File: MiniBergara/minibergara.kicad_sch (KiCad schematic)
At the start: 12 parts, among them SW1 SW_Nidec_CAS-120A1, U1 TB6612_BREAKOUT, U3 AMS1117-1.5

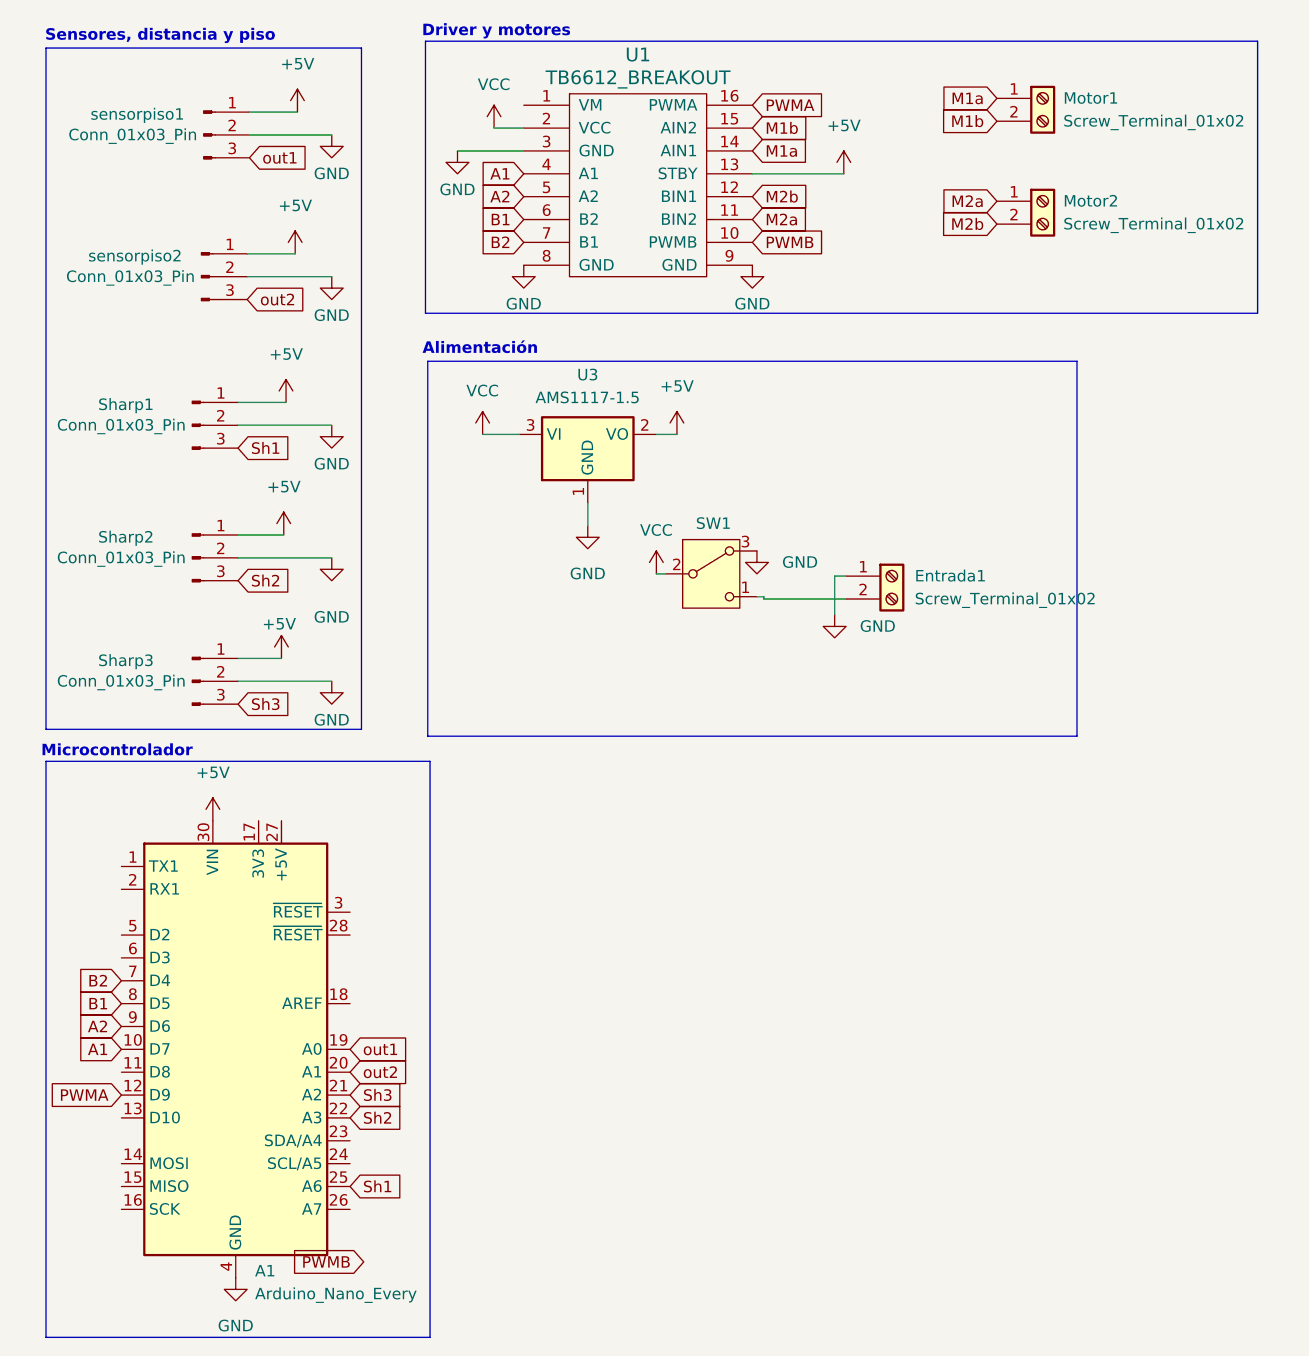
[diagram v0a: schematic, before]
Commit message: falta mover nano
move el nano abajo con las pistas
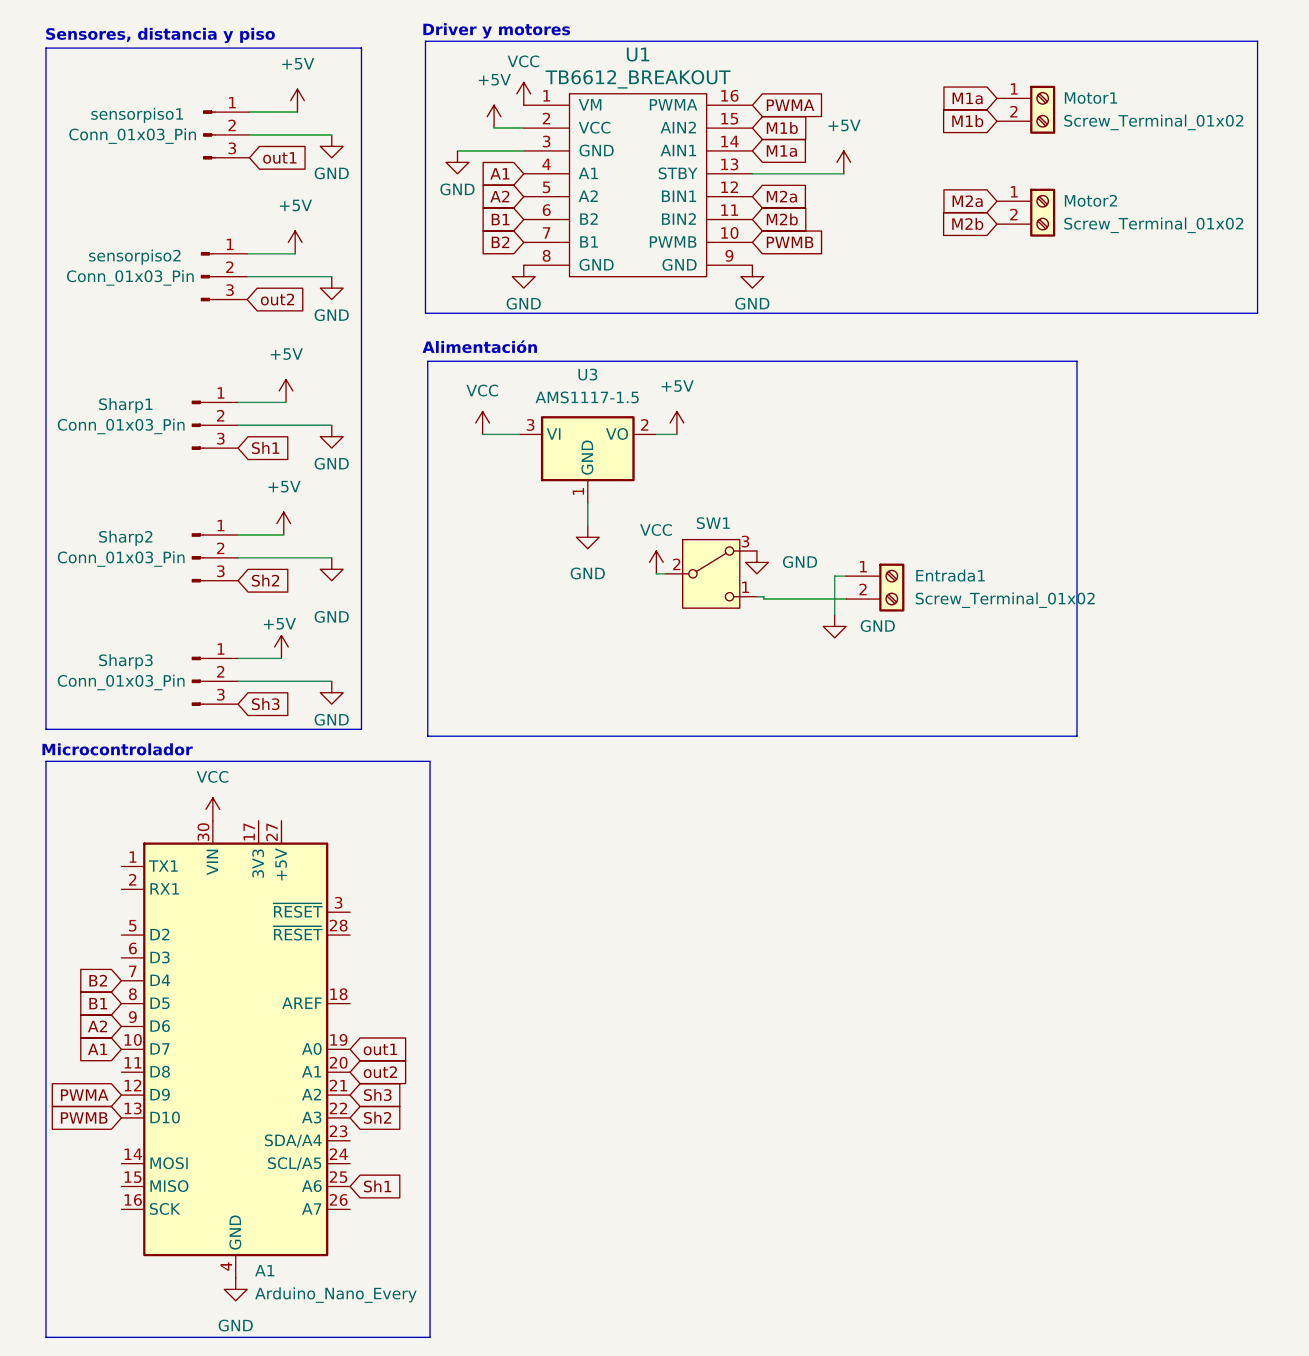
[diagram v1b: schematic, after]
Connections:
- net +5V: now also U1.2 (VCC); no longer A1.30 (VIN)
- net M2a: now also U1.12 (BIN1); no longer U1.11 (BIN2)
- net M2b: now also U1.11 (BIN2); no longer U1.12 (BIN1)
- net PWMB: now also A1.13 (D10)
- net VCC: now also A1.30 (VIN), U1.1 (VM); no longer U1.2 (VCC)
